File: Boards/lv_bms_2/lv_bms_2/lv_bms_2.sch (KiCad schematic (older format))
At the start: 114 parts, among them J1 CONN_02X03, J10 NanoFit_RA_TH_04, J2 NanoFit_RA_TH_06, J4 NanoFit_RA_TH_02, J5 NanoFit_RA_TH_02, J6 NanoFit_RA_TH_02, J7 NanoFit_RA_TH_02, J8 NanoFit_RA_TH_02, J9 NanoFit_RA_TH_02, Q1 NSS1C201MZ4, Q2 SQM110P06, Q3 MMBF170, Q4 MMBF170, Q5 SQM110P06, U1 MCP2561-E_SN, U10 ACHS-7124, U11 redcube-7461057, U2 ATMEGA16M1, U3 LTC6810HG-1, U4 LT3066IMSE-5, U5 LT1017IS8, U6 R_500, U7 R_500, U8 R_500, U9 redcube-7461057, Y1 Crystal_SMD

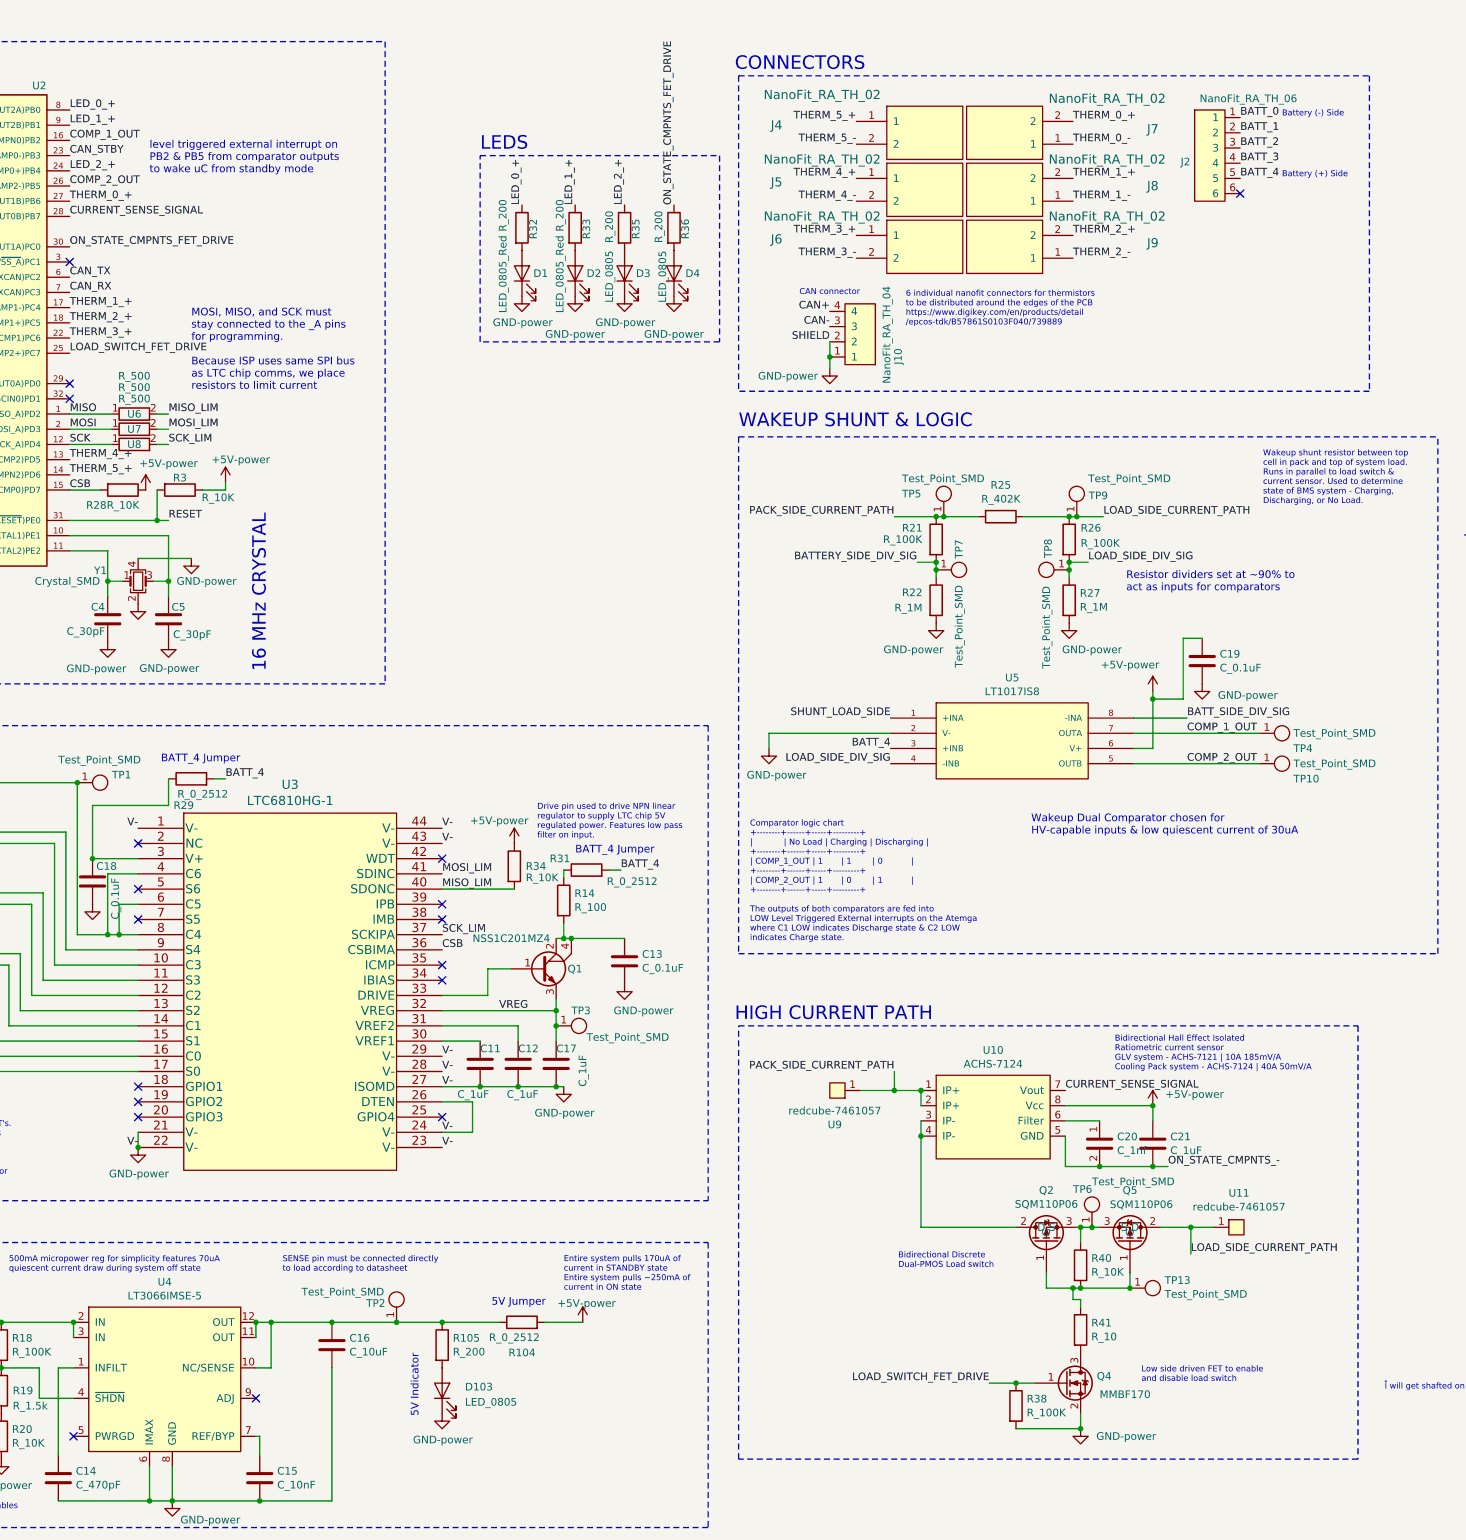
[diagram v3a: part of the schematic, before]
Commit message: lv bms updates
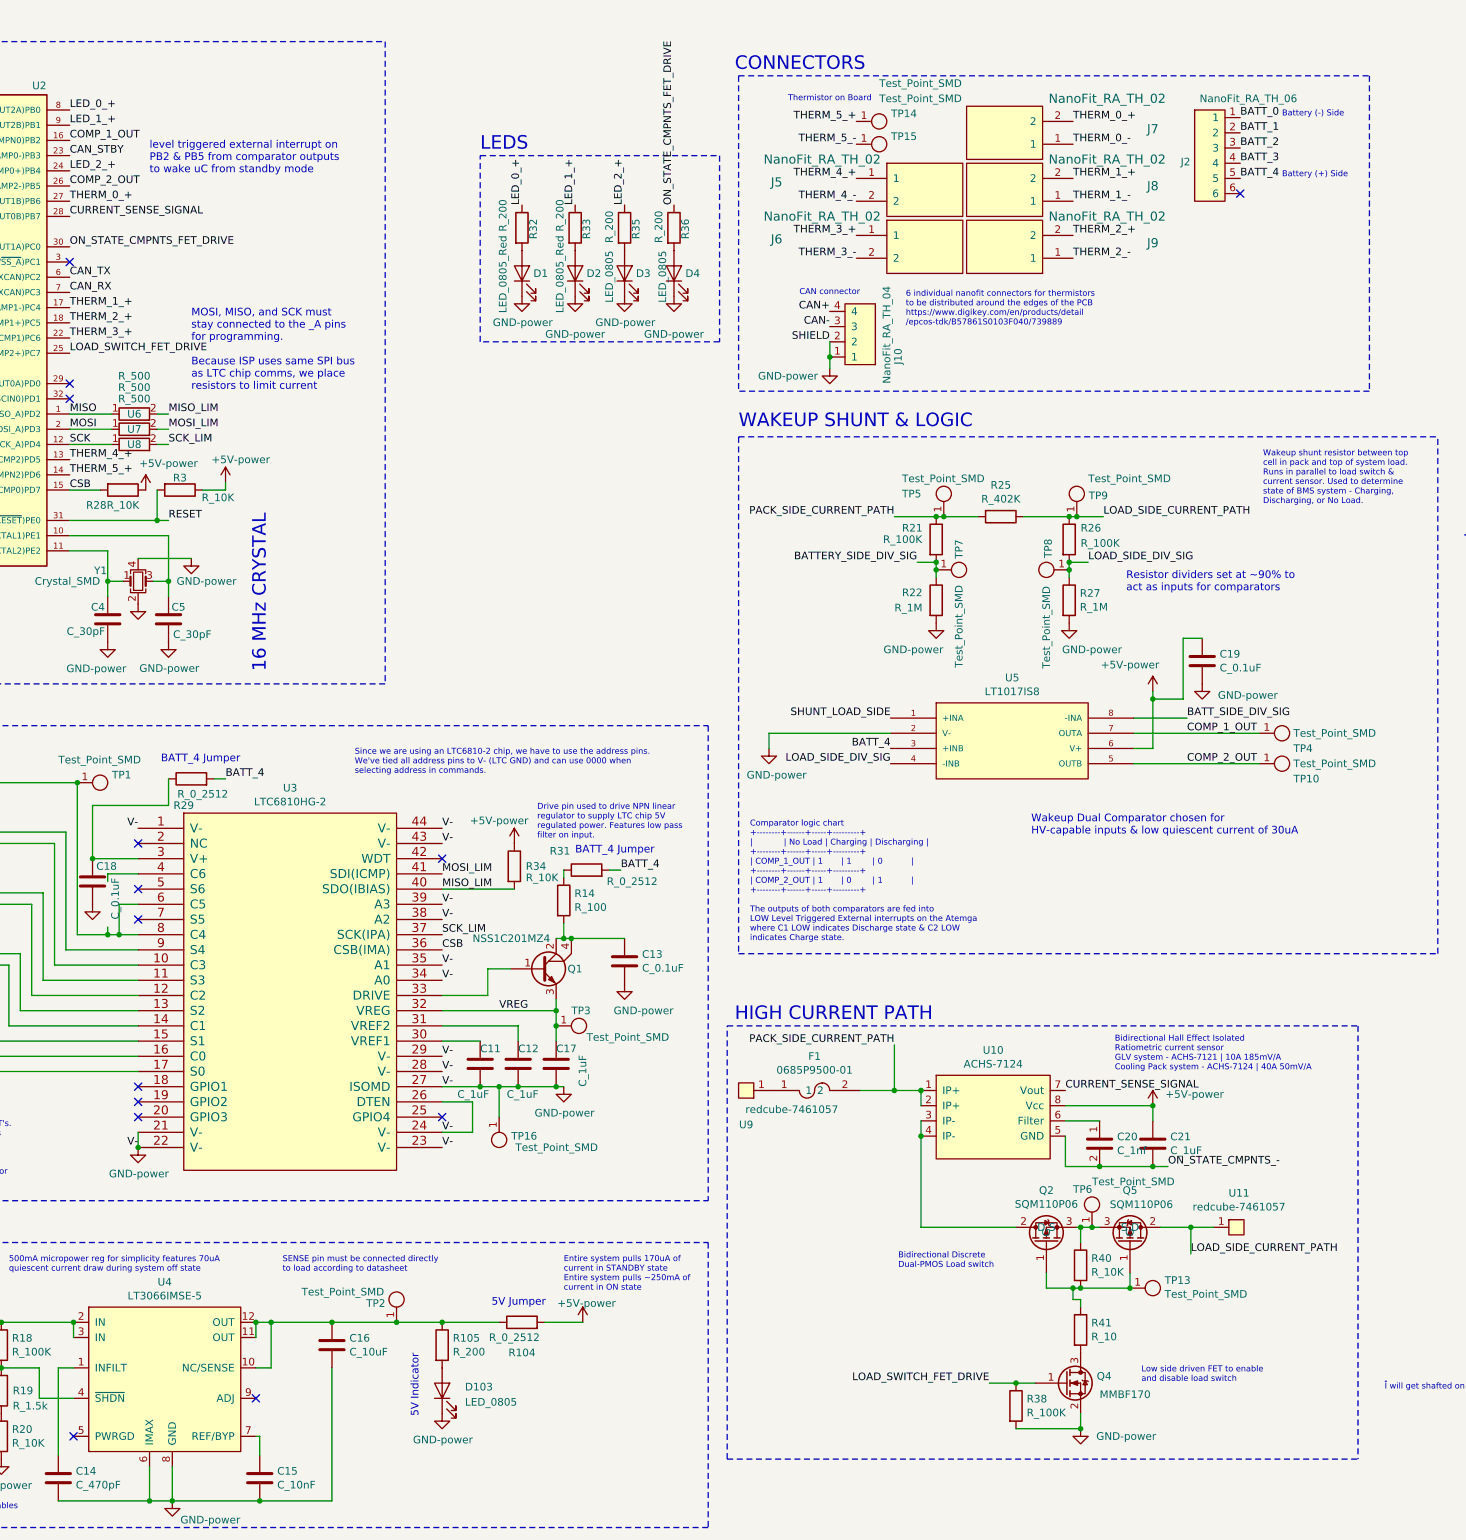
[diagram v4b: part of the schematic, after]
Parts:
- removed J4: NanoFit_RA_TH_02, footprints:NanoFit_Molex_1x02x2.50mm_Angled_OEM, symbol formula:NanoFit_RA_TH_02
- removed U3: LTC6810HG-1, formula:LTC6810HG-1, symbol formula:LTC6810HG-1
- added F1: 0685P9500-01, footprints:Fuse_1206, symbol formula:0685P9500-01
- added TP14, TP15, TP16: Test_Point_SMD, footprints:Test_Point_SMD, symbol formula:Test_Point_SMD
- added U3: LTC6810HG-2, footprints:SOP50P780X200-44N, symbol formula:LTC6810HG-2
- C20: footprint formula:C_0805_OEM -> footprints:C_0805_OEM
- Q2, Q5: footprint formula:TO-263-2-Heatsink -> footprints:TO-263-3-TabPin2
- Q3, Q4: footprint TO_SOT_Packages_SMD:SOT-23 -> footprints:SOT-23-3_OEM
- R4, R5, R6, R7, R8: footprint formula:356030RFT -> footprints:356030RFT
- U10: footprint formula:OPTO_HCPL-070A-000E -> footprints:OPTO_HCPL-070A-000E
- U11, U9: footprint formula:redcube_pressfit_6pin -> footprints:redcube_pressfit_6pin
- U4: footprint formula:MSOP-8 -> footprints:MSOP-12_MSE
- U5: footprint formula:SO-8_S -> footprints:SO-8_S
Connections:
- net CSB: now also U3.36 (CSB(IMA))
- net GND: now also TP16.1, U3.1 (V-), U3.21 (V-), U3.22 (V-), U3.23 (V-), U3.24 (V-), U3.26 (DTEN), U3.27 (ISOMD), U3.28 (V-), U3.29 (V-), U3.34 (A0), U3.35 (A1), U3.38 (A2), U3.39 (A3), U3.43 (V-), U3.44 (V-)
- net MISO_LIM: now also U3.40 (SDO(IBIAS))
- net MOSI_LIM: now also U3.41 (SDI(ICMP))
- net ON_STATE_CMPNTS_-: now also TP15.1
- net PACK_SIDE_CURRENT_PATH: now also F1.2; no longer U9.1
- net SCK_LIM: now also U3.37 (SCK(IPA))
- net THERM_5_+: now also TP14.1
- net VREG: now also U3.32 (VREG)
- net at Q1.1: now also U3.33 (DRIVE)
- net at C10.1, C9.2, R13.1: now also U3.16 (C0)
- net at C10.2, R8.1: now also U3.17 (S0)
- net at C8.2, C9.1, R12.1: now also U3.14 (C1)
- net at C7.2, C8.1, R11.1: now also U3.12 (C2)
- net at C6.2, C7.1, R10.1: now also U3.10 (C3)
- net at C6.1, R9.1, TP1.1: now also U3.6 (C5), U3.8 (C4)
- net at C12.1: now also U3.31 (VREF2)
- net at C11.1: now also U3.30 (VREF1)
- net at R6.1: now also U3.13 (S2)
- net at R7.1: now also U3.15 (S1)
- net at R5.1: now also U3.11 (S3)
- net at R4.1: now also U3.9 (S4)
- net at C18.2, R29.1: now also U3.3 (V+)
- new net: F1.1, U9.1
- no-connect marks 20 -> 16
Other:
- note added: "Since we are using an LTC6810-2 chip, we have to use the address pins.\nWe've tied all address pins to V- (LTC GND) and can use 0000 when\nselecting address in commands."
- note added: "Thermistor on Board"
- moved on the sheet: U9

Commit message: lv_bms_2 DR review changes
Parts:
- removed Q3, Q4: MMBF170, footprints:SOT-23-3_OEM, symbol formula:MMBF170
- added J3: NanoFit_RA_TH_02, footprints:NanoFit_Molex_1x02x2.50mm_Angled_OEM, symbol formula:NanoFit_RA_TH_02
- added Q3, Q4, Q6: BSS138, Package_TO_SOT_SMD:SOT-23, symbol Transistor_FET:BSS138
- added R42: R_100K, footprints:R_0805_OEM, symbol formula:R_100K
- added TP17: Test_Point_SMD, footprints:Test_Point_SMD, symbol formula:Test_Point_SMD
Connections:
- net +5V: now also J3.2
- net GND: now also Q4.2 (S), Q6.2 (S), R42.2; no longer R39.2
- net LOAD_SWITCH_FET_DRIVE: now also Q6.1 (G)
- net ON_STATE_CMPNTS_-: now also Q3.3 (D)
- net ON_STATE_CMPNTS_FET_DRIVE: now also Q3.1 (G)
- net FAN_PWM: now reaches U2.3 ((PCINT9/PSCIN1/OC1B/~SS_A~)PC1)
- net FAN_PWM: now also Q4.1 (G), R42.1
- net at C6.1, R9.1, TP1.1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: now also U3.4 (C6)
- net at R41.2: now also Q6.3 (D)
- new net: Q3.2 (S), R39.2
- new net FAN_PWM_LSD: J3.1, Q4.3 (D), TP17.1
- no-connect marks 16 -> 15
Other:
- note added: "LSD FET's"
- note added: "Low side driven FET to toggle external \nrelay for FAN PWM. Likely won't use\nthis feature, backup incase of poor\nPCB thermal performance in Cooling \nPack"
- note added: "The high current path on this \nPCB will see 20A continuous, \n30A peak for 1 hour with the \ncooling pack, and 5A continuous \nwith the GLV pack. Our high \ncurrent path features a current \nsensor, bidirectional load switch, \nand fuse. \n\nThe fuse and current sensor are \nswappable between GLV system \nand cooling pack system. \n\nThe bidirectional load switch was \ntested with the LV BMS Tes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"
- note removed: "FET"
